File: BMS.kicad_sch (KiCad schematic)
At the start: 6 parts, among them U2 MCP73831T-5ACI_OT

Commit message: Add BMS
Signed-off-by: JeffMboya <jangina.mboya@gmail.com>
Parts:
- added C10, C9: 10uF, Capacitor_SMD:C_1206_3216Metric, symbol Device:C
- added D7: 1N5819HW-7-F, 1N5819HW-7-F:SOD3715X145N, symbol 1N5819HW-7-F:1N5819HW-7-F
- added Q4: SSM3J328R_LF, SSM3J328R_LF:SOT95P240X88-3N, symbol SSM3J328R_LF:SSM3J328R_LF
- added R13, R14: 10k, Resistor_SMD:R_0603_1608Metric, symbol Device:R
- added R15, R16: 100k, Resistor_SMD:R_0603_1608Metric, symbol Device:R
- added U3: XC6220B331PR-G, symbol XC6220B331PR-G:XC6220B331PR-G
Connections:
- net +5V: now also D7.A, Q4.1 (G), R13.1
- net +BATT: now also Q4.3 (D), R15.2
- net GND: now also C10.1, C9.2, R13.2, R16.1, U3.2 (VSS)
- new net +3V3: C10.2, U3.5 (VOUT)
- new net BATT_MON: R15.1, R16.2
- new net CE: R14.2, U3.1 (CE)
- new net VIN: C9.1, D7.C, Q4.2 (S), R14.1, U3.4 (VIN)
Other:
- moved on the sheet: C7, C8, D6, R11, R12, U2

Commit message: Add BMS
Signed-off-by: JeffMboya <jangina.mboya@gmail.com>
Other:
- company: (none) -> ABDTRACT MACHINES
- title: (none) -> BMS
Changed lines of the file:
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@@
 	(generator_version "8.0")
 	(paper "A4")
+	(title_block
+		(title "BMS")
+		(date "20 NOV 2024")
+		(rev "1")
+		(company "ABDTRACT MACHINES")
+		(comment 1 "DRAWN BY: JEFF MBOYA")
+		(comment 2 "APPROVED BY:")
+	)
 	(junction
 		(at 143.51 53.34)

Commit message: Update PCB
Signed-off-by: JeffMboya <jangina.mboya@gmail.com>
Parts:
- removed U3: XC6220B331PR-G, symbol XC6220B331PR-G:XC6220B331PR-G
- added U5: XC6220B331PR-G, symbol XC6220B331PR-G:XC6220B331PR-G
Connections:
- net +3V3: now also U5.5 (VOUT)
- net CE: now also U5.1 (CE)
- net GND: now also U5.2 (VSS)
- net VIN: now also U5.4 (VIN)

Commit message: Add battery socket
Signed-off-by: JeffMboya <jangina.mboya@gmail.com>
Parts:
- added BT1: BAT-HLD-006-SMT, BAT-HLD-006-SMT:BAT_BAT-HLD-006-SMT, symbol BAT-HLD-006-SMT:BAT-HLD-006-SMT
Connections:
- net +BATT: now also BT1.P1, BT1.P2
- net GND: now also BT1.N
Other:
- moved on the sheet: R15, R16

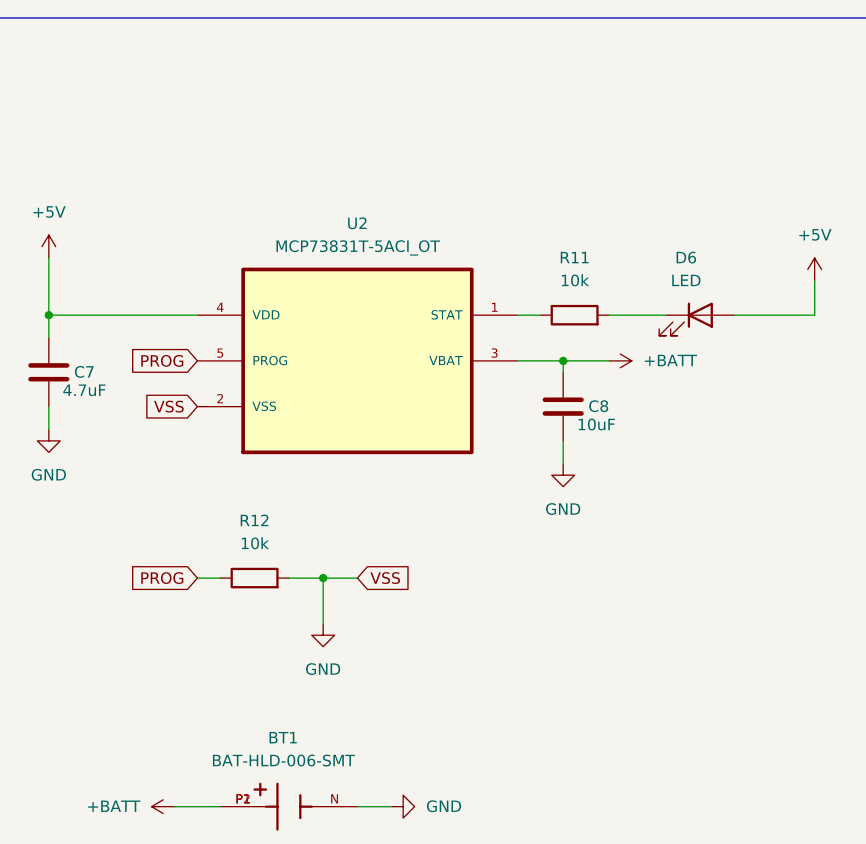
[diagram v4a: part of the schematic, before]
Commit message: Add coin battery holder
Signed-off-by: JeffMboya <jangina.mboya@gmail.com>
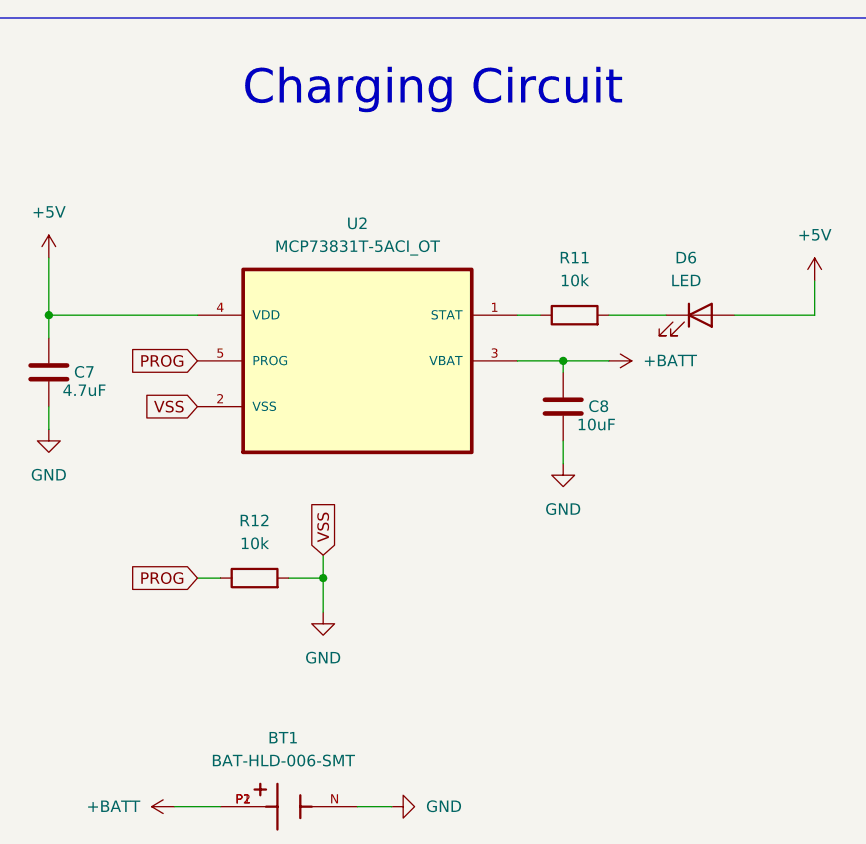
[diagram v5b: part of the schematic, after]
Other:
- note added: "Charging Circuit"
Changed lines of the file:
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@@
-	(wire
-		(pts
-			(xy 59.69 88.9) (xy 55.88 88.9)
-		)
-		(stroke
-			(width 0)
-			(type default)
-		)
-	)
 	(wire
 		(pts
@@
 	(wire
 		(pts
+			(xy 55.88 86.36) (xy 55.88 88.9)
+		)
+		(stroke
+			(width 0)
+			(type default)
+		)
+	)
+	(wire
+		(pts
 			(xy 165.1 74.93) (xy 165.1 78.74)
 		)
@@
 	(wire
 		(pts
-			(xy 55.88 93.98) (xy 55.88 88.9)
+			(xy 55.88 92.71) (xy 55.88 88.9)
 		)
 		(stroke
@@
 		)
 	)
+	(text "Charging Circuit"
+		(exclude_from_sim no)
+		(at 68.072 34.544 0)
+		(effects
+			(font
+				(size 3.81 3.81)
+			)
+		)
+	)
 	(global_label "VOUT"
 		(shape input)
@@
 	(global_label "VSS"
 		(shape input)
-		(at 59.69 88.9 0)
+		(at 55.88 86.36 90)
 		(fields_autoplaced yes)
 		(effects
@@
 		)
 		(property "Intersheetrefs" "${INTERSHEET_REFS}"
-			(at 66.1828 88.9 0)
+			(at 55.88 79.8672 90)
 			(effects
 				(font
@@
 	(symbol
 		(lib_id "power:GND1")
-		(at 55.88 93.98 0)
+		(at 55.88 92.71 0)
 		(unit 1)
 		(exclude_from_sim no)
@@
 		(fields_autoplaced yes)
 		(property "Reference" "#PWR027"
-			(at 55.88 100.33 0)
+			(at 55.88 99.06 0)
 			(effects
 				(font
@@
 		)
 		(property "Value" "GND"
-			(at 55.88 99.06 0)
+			(at 55.88 97.79 0)
 			(effects
 				(font
@@
 		)
 		(property "Footprint" ""
-			(at 55.88 93.98 0)
+			(at 55.88 92.71 0)
 			(effects
 				(font
@@
 		)
 		(property "Datasheet" ""
-			(at 55.88 93.98 0)
+			(at 55.88 92.71 0)
 			(effects
 				(font
@@
 		)
 		(property "Description" "Power symbol creates a global label with name \"GND1\" , ground"
-			(at 55.88 93.98 0)
-			(effects
-				(font
+			(at 55.88 92.71 0)
+			(effects
+				(font

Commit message: Add JST
Signed-off-by: JeffMboya <jangina.mboya@gmail.com>
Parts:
- removed BT1: BAT-HLD-006-SMT, BAT-HLD-006-SMT:BAT_BAT-HLD-006-SMT, symbol BAT-HLD-006-SMT:BAT-HLD-006-SMT
- added J3: BM02B-SRSS-TB_LF__SN_, BM02B-SRSS-TB_LF__SN_:JST_BM02B-SRSS-TB_LF__SN_, symbol BM02B-SRSS-TB_LF__SN_:BM02B-SRSS-TB_LF__SN_
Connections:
- net +BATT: now also J3.1
- net GND: now also J3.2, J3.S1 (SHIELD), J3.S2 (SHIELD)

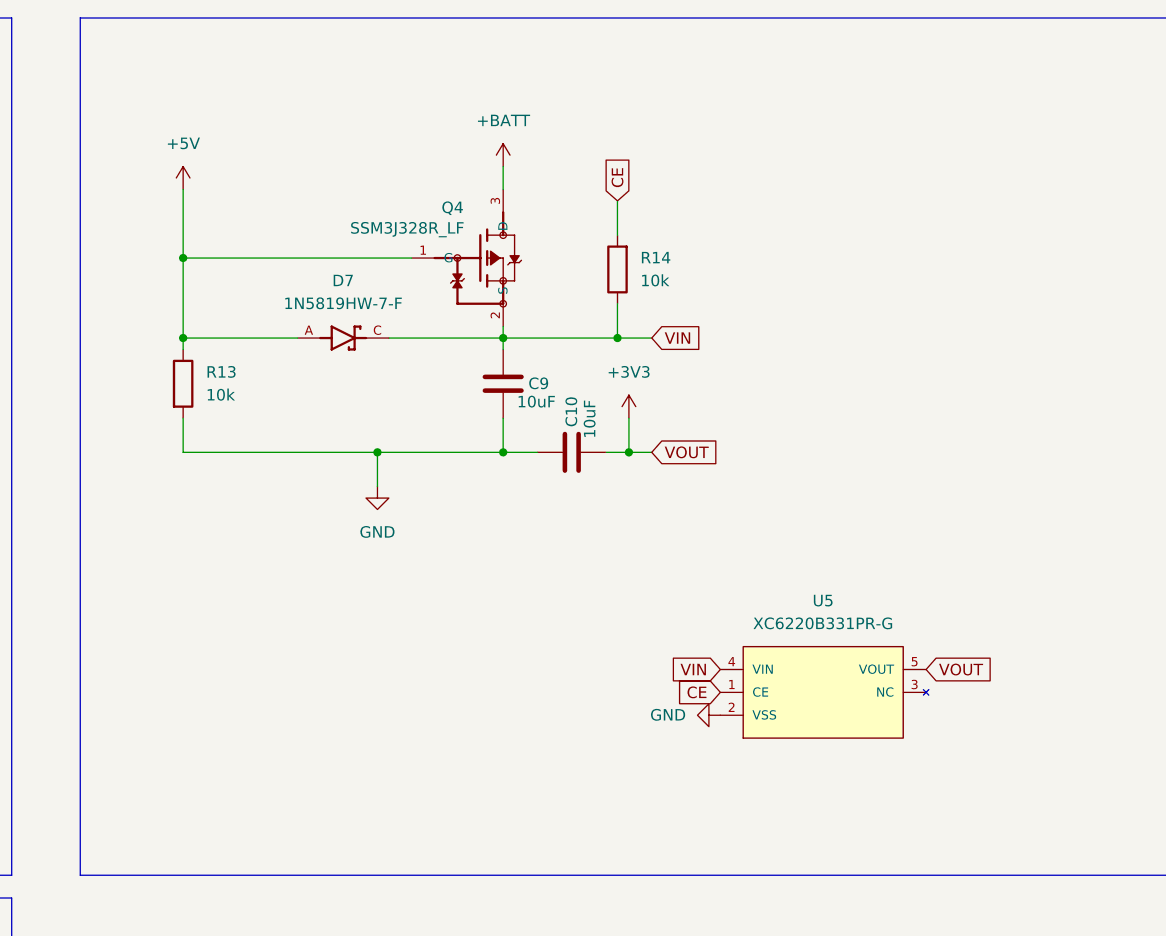
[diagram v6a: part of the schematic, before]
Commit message: Delete all tracks
Signed-off-by: JeffMboya <jangina.mboya@gmail.com>
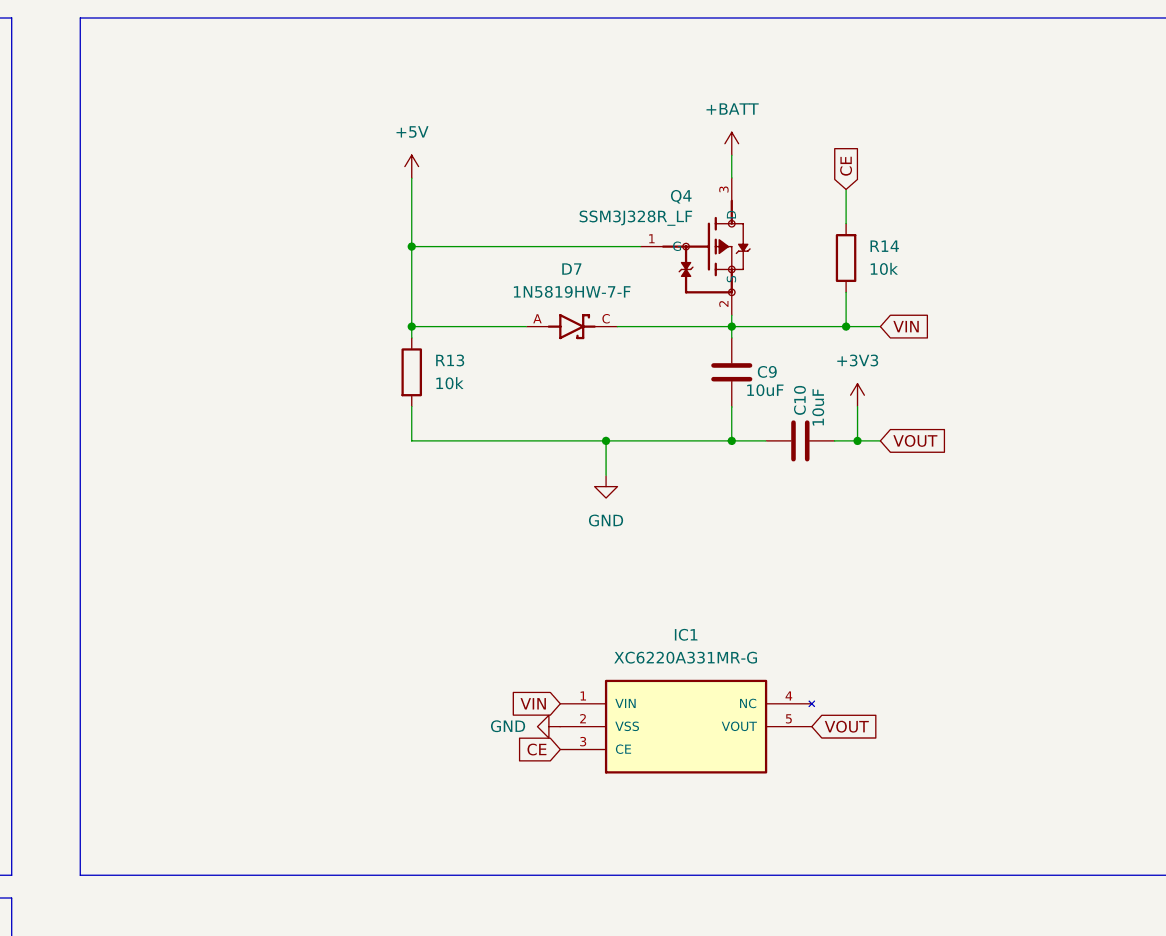
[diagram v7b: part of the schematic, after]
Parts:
- removed U5: XC6220B331PR-G, symbol XC6220B331PR-G:XC6220B331PR-G
- added IC1: XC6220A331MR-G, XC6220A331MR-G:SOT95P280X120-5N, symbol XC6220A331MR-G:XC6220A331MR-G
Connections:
- net +3V3: now also IC1.5 (VOUT)
- net CE: now also IC1.3 (CE)
- net GND: now also IC1.2 (VSS)
- net VIN: now also IC1.1 (VIN)
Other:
- moved on the sheet: C10, C9, D7, Q4, R13, R14
